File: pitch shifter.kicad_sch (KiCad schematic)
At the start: 16 parts, among them J1 MOLEX_430450412, J2 MOLEX_436500315, U2 STM32G030K8T6, U3 PCM3060PWR, Y1 ASE24LRT

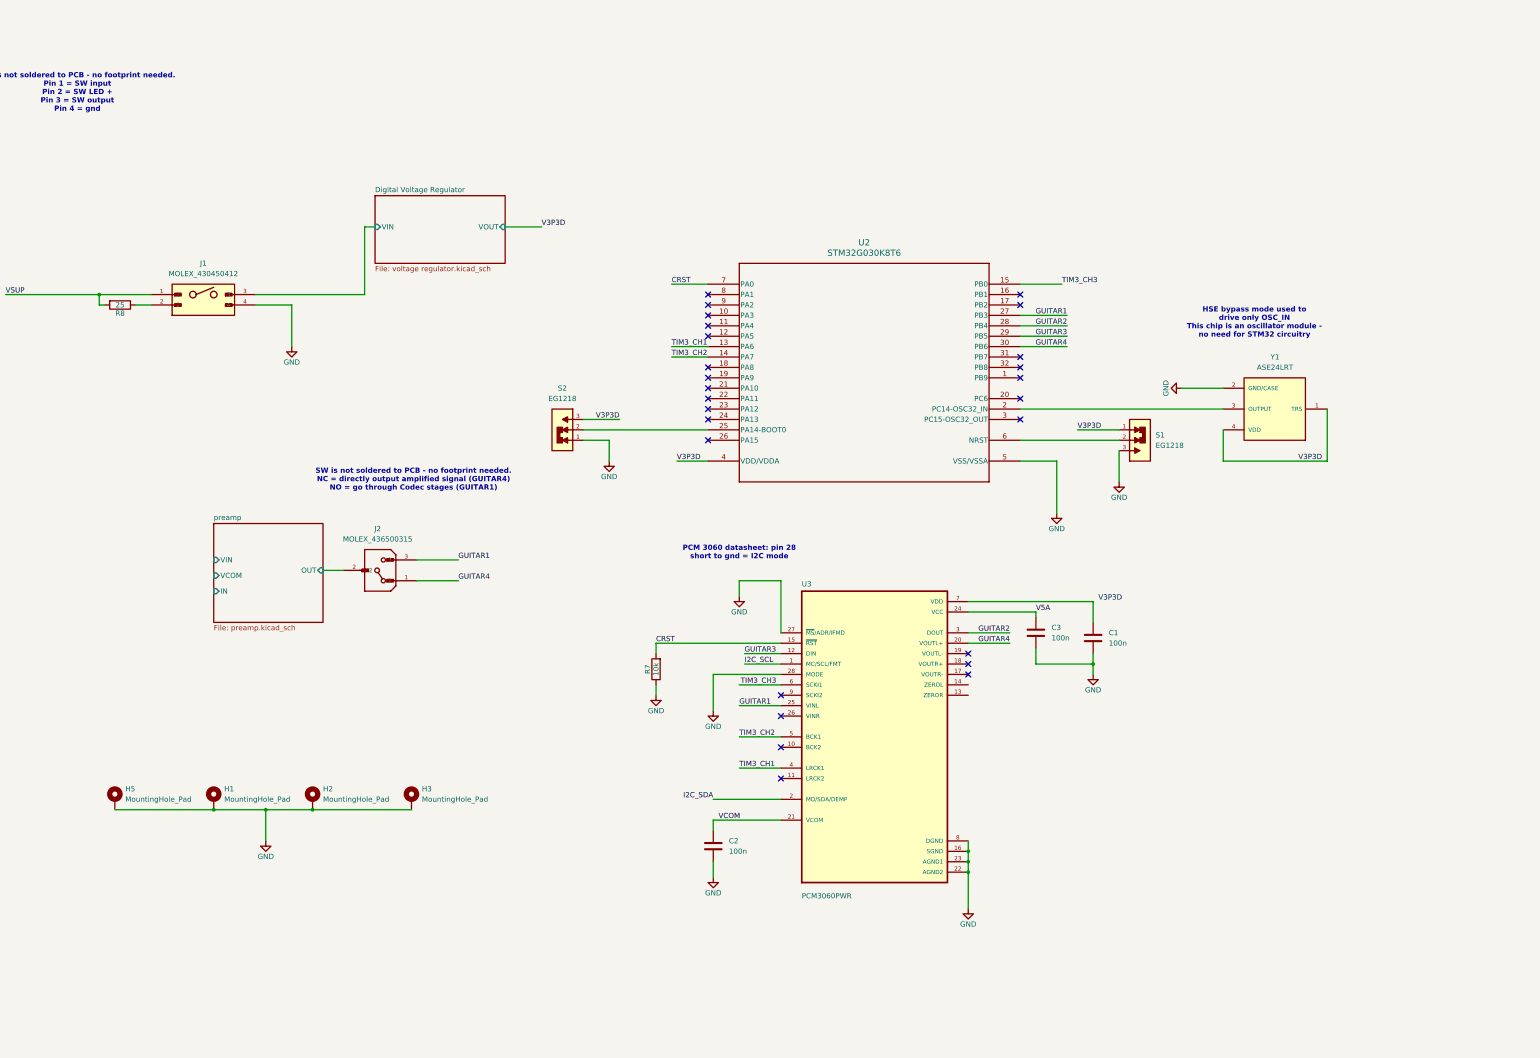
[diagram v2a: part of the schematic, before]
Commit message: Added analog supply, finished codec wiring, added audio jacks
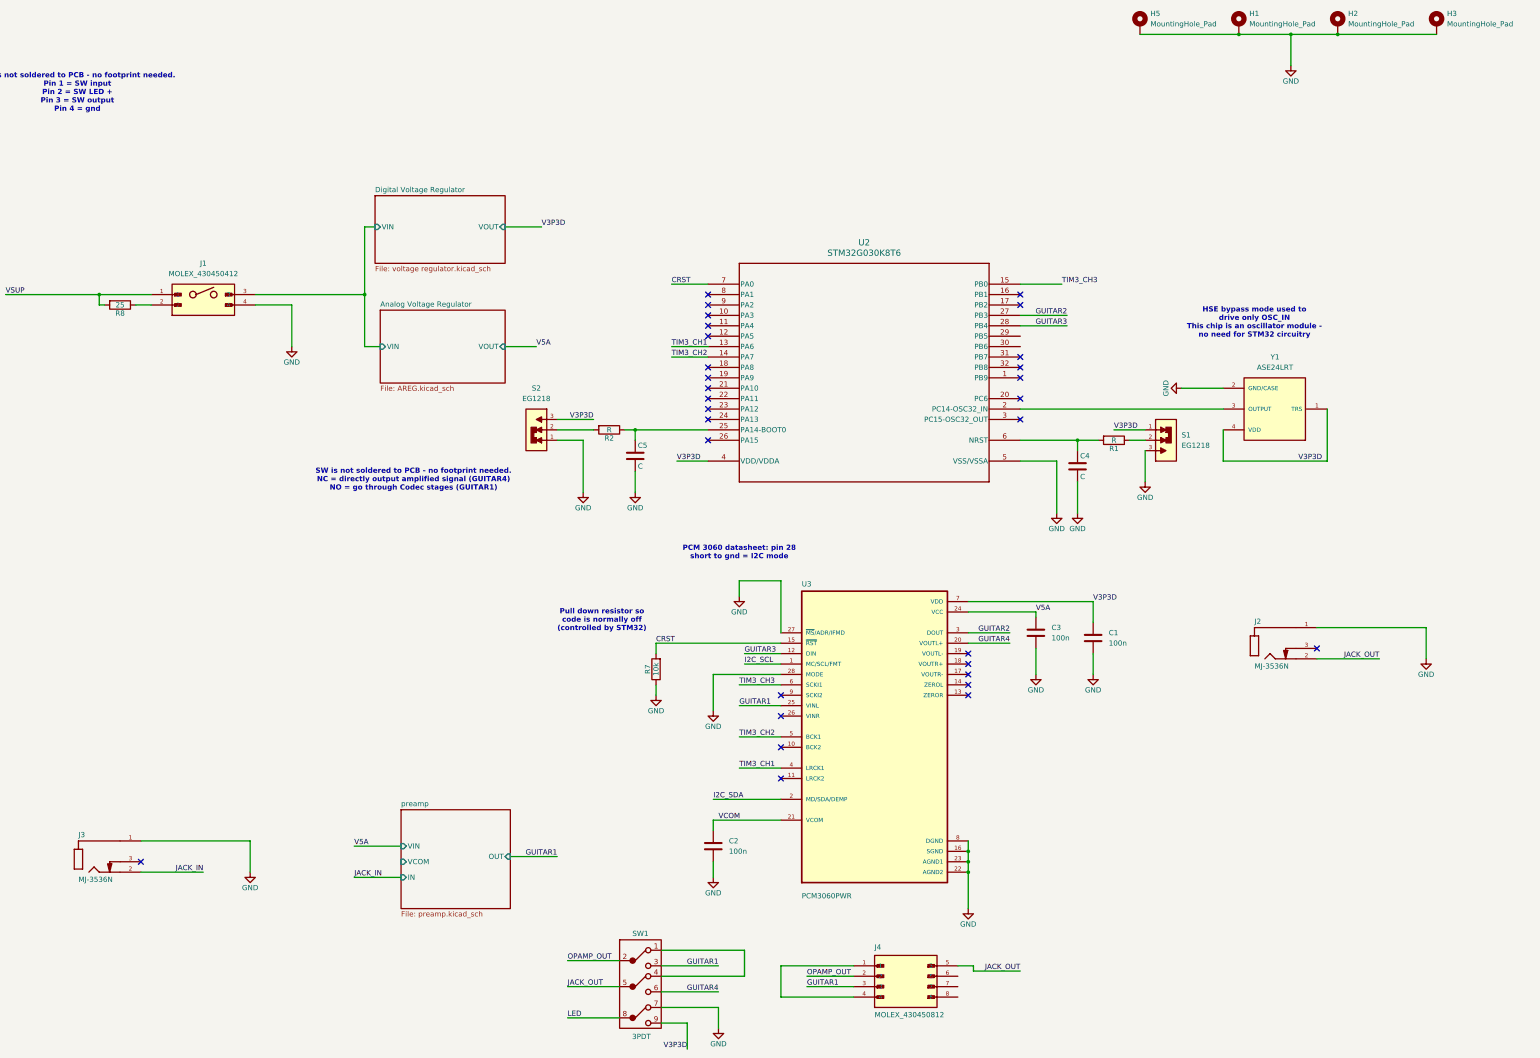
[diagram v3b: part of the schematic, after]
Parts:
- removed J2: MOLEX_436500315, Project_Components:MOLEX_436500315, symbol Project_Components:MOLEX_436500315
- added C4, C5: C, symbol Device:C
- added J2, J3: MJ-3536N, Project_Components:MJ-3536N, symbol Project_Components:MJ-3536N
- added J4: MOLEX_430450812, Project_Components:MOLEX_430450812, symbol Project_Components:MOLEX_430450812
- added R1, R2: R, symbol Device:R
- added SW1: 3PDT, symbol Project_Components:3PDT
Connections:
- net GND: now also C4.2, C5.2, J2.1, J3.1, SW1.7
- net GUITAR1: now also J4.3, SW1.3; no longer U2.27 (PB3)
- net GUITAR2: now also U2.27 (PB3); no longer U2.28 (PB4)
- net GUITAR3: now also U2.28 (PB4); no longer U2.29 (PB5)
- net GUITAR4: now also SW1.6; no longer U2.30 (PB6)
- net V3P3D: now also C1.1, U3.7 (VDD), SW1.9
- net at U2.25 (PA14-BOOT0): now also C5.1, R2.1; no longer S2.2
- net at S1.2: now also R1.1; no longer U2.6 (NRST)
- net Digital Voltage Regulator/VIN renamed Analog Voltage Regulator/VIN
- new net: C4.1, R1.2, U2.6 (NRST)
- new net: R2.2, S2.2
- new net: J4.1, J4.4
- new net: SW1.1, SW1.4
- new net JACK_IN: J3.2
- new net JACK_OUT: J2.2, J4.5, SW1.5
- new net LED: SW1.8
- new net OPAMP_OUT: J4.2, SW1.2
- no-connect marks 26 -> 30
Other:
- added sheet Analog Voltage Regulator (AREG.kicad_sch)
- note added: "Pull down resistor so code is normally off (controlled by STM32)"
- moved on the sheet: H1, H2, H3, H5, S1, S2

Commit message: swap stm32 with SAI compatible and add new molex connector
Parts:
- removed C5: C, symbol Device:C
- removed J4: MOLEX_430450812, Project_Components:MOLEX_430450812, symbol Project_Components:MOLEX_430450812
- removed R2: R, symbol Device:R
- removed S2: EG1218, Project_Components:EG1218, symbol Project_Components:EG1218
- removed U2: STM32G030K8T6, Project_Components:STM32G030K8T6, symbol Project_Components:STM32G030K8T6
- added C18: C, symbol Device:C
- added D3: D, symbol Device:D
- added J4: MOLEX_430450612, Project_Components:MOLEX_430450612, symbol Project_Components:MOLEX_430450612
- added R13, R14: R, symbol Device:R
- added S3: EG1218, Project_Components:EG1218, symbol Project_Components:EG1218
- added U6: STM32L432KCU6, Project_Components:STM32L432KCU6, symbol Project_Components:STM32L432KCU6
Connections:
- net GND: now also C18.2, D3.1 (K), S3.1, U6.16 (VSS), U6.32 (VSS__1); no longer SW1.7
- net GUITAR1: now also J4.2
- net GUITAR4: now also J4.4
- net JACK_OUT: now also J4.3
- net OPAMP_OUT: now also J4.1
- net V3P3D: now also J4.6, S3.3
- net at C4.1, R1.2: now also U6.4 (NRST)
- net at Y1.3 (OUTPUT): now also U6.2 (PC14-OSC32_1N)
- new net: C18.1, R14.2, U6.31 (PH3/BOOT0)
- new net: D3.2 (A), R13.1
- new net: J4.5, R13.2
- new net: R14.1, S3.2
- no-connect marks 30 -> 13
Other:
- note added: "This 3PDT switch is panel mounted (not on board) so it is merely a representation of the connections"
- moved on the sheet: C4, R1, S1, SW1, Y1

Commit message: Complete pre-amp and pre-amp sim
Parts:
- removed J1: MOLEX_430450412, Project_Components:MOLEX_430450412, symbol Project_Components:MOLEX_430450412
- removed J2, J3: MJ-3536N, Project_Components:MJ-3536N, symbol Project_Components:MJ-3536N
- removed R1: R, symbol Device:R
- removed S1, S3: EG1218, Project_Components:EG1218, symbol Project_Components:EG1218
- added C19: 1u, Capacitor_SMD:C_0201_0603Metric_Pad0.64x0.40mm_HandSolder, symbol Device:C
- added C20, C5: 10n, Capacitor_SMD:C_0201_0603Metric_Pad0.64x0.40mm_HandSolder, symbol Device:C
- added C21: 4.7u, Capacitor_SMD:C_0201_0603Metric_Pad0.64x0.40mm_HandSolder, symbol Device:C
- added C22: 100n, Capacitor_SMD:C_0201_0603Metric_Pad0.64x0.40mm_HandSolder, symbol Device:C
- added J5: SBH11-PBPC-D05-ST-BK, Project_Components:SBH11-PBPC-D05-ST-BK, symbol Project_Components:SBH11-PBPC-D05-ST-BK
- added R15, R2: 4.7k, symbol Device:R
- added SW2: PTS636, Project_Components:PTS636, symbol Project_Components:PTS636
- added SW3: EG1218, Project_Components:EG1218, symbol Project_Components:EG1218
- added SW5: SW_DPST, symbol Switch:SW_DPST
- C18, C4: value C -> 100n
- D3: footprint (none) -> Diode_SMD:D_0603_1608Metric_Pad1.05x0.95mm_HandSolder
- R13: value R -> 47
- R14: value R -> 10k
- R8: value 25 -> 47
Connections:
- net I2C_SCL is gone; now on net I2C_SCLK: U3.1 (MC/SCL/FMT)
- net TIM3_CH1 is gone; now on net WSCLK: U3.4 (LRCK1)
- net TIM3_CH2 is gone; now on net BLCK: U3.5 (BCK1)
- net TIM3_CH3 is gone; now on net SYSCLK: U3.6 (SCKI1)
- net Analog Voltage Regulator/VIN: now also SW5.4
- net CRST: now also U6.19 (PA9)
- net GND: now also U6.33 (EXP), C19.2, C20.2, C21.2, C22.2, C5.2, J5.5 (GND), J5.6 (GND), SW2.1 (A), SW3.1, SW5.2
- net GUITAR2: now also U6.20 (PA10)
- net GUITAR3: now also U6.28 (PB5)
- net I2C_SDA: now also U6.30 (PB7), R15.2
- net V3P3D: now also U6.1 (VDD), U6.17 (VDD__1), C20.1, C21.1, C22.1, J5.7 (3.3V), J5.8 (3.3V), R15.1, R2.1, SW3.3
- net V5A: now also U6.5 (VDDA/VREF+), C19.1, C5.1
- net VSUP: now also SW5.3
- net STRST: now reaches C4.1, U6.4 (NRST)
- net STRST: now also J5.1 (RST), SW2.2 (B)
- net SWDIO: now reaches U6.23 (PA13/JTMS-SWDIO)
- net SWDIO: now also J5.4 (SWDIO)
- net SWCLK: now reaches U6.24 (PA14/JTCK-SWCLK)
- net SWCLK: now also J5.2 (SWCLK)
- net I2C_SCLK: now reaches U6.29 (PB6)
- net I2C_SCLK: now also R2.2
- net WSCLK: now reaches U6.6 (PA0/CK_IN)
- net BLCK: now reaches U6.7 (PA1)
- net SYSCLK: now reaches U6.8 (PA2)
- net at R14.1: now also SW3.2
- net at R8.1: now also SW5.1
- no-connect marks 13 -> 27
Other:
- sheet preamp ports: added none; removed VCOM
- note added: "1 100n for each VDD pin"
- note added: "I2C pull up resistors"
- note added: "Pull down resistor so codec is normally off (controlled by STM32)"
- note removed: "Pull down resistor so code is normally off (controlled by STM32)"
- moved on the sheet: C18, C4, D3, R13, R14, R8, U6, Y1

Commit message: Began board layout
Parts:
- removed D3: D, Diode_SMD:D_0603_1608Metric_Pad1.05x0.95mm_HandSolder, symbol Device:D
- removed J4: MOLEX_430450612, Project_Components:MOLEX_430450612, symbol Project_Components:MOLEX_430450612
- removed R13: 47, symbol Device:R
- added D1: D, Diode_SMD:D_0603_1608Metric_Pad1.05x0.95mm_HandSolder, symbol Device:D
- added J1: TBL002A-4, Project_Components:TBL002A-4, symbol Project_Components:TBL002A-4
- added J2: USB4125-GF-A, Project_Components:USB-C (power only), symbol Project_Components:USB-C (power only)
- added J3: TBL002A-10, Project_Components:TBL002A-10, symbol Project_Components:TBL002A-10
- added R1, R5: 47, Resistor_SMD:R_0603_1608Metric_Pad0.98x0.95mm_HandSolder, symbol Device:R
- added R3, R4: 5.1k, Resistor_SMD:R_0603_1608Metric_Pad0.98x0.95mm_HandSolder, symbol Device:R
- added TP1, TP10, TP11, TP12, TP13, TP14, TP15, TP16, TP17, TP18, TP19, TP2, TP20, TP21, TP22, TP23, TP24, TP25, TP26, TP27, TP28, TP29, TP3, TP30, TP4, TP5, TP6, TP7, TP8, TP9: Test Point, TestPoint:TestPoint_THTPad_D1.0mm_Drill0.5mm, symbol Project_Components:Inline Test Point
- C1: renamed from C2; footprint Capacitor_SMD:C_0201_0603Metric_Pad0.64x0.40mm_HandSolder -> Capacitor_SMD:C_0603_1608Metric_Pad1.08x0.95mm_HandSolder
- C10: renamed from C21; footprint Capacitor_SMD:C_0201_0603Metric_Pad0.64x0.40mm_HandSolder -> Capacitor_SMD:C_0603_1608Metric_Pad1.08x0.95mm_HandSolder
- C2: renamed from C4; footprint (none) -> Capacitor_SMD:C_0603_1608Metric_Pad1.08x0.95mm_HandSolder
- C3: footprint Capacitor_SMD:C_0201_0603Metric_Pad0.64x0.40mm_HandSolder -> Capacitor_SMD:C_0603_1608Metric_Pad1.08x0.95mm_HandSolder
- C4: renamed from C1; footprint Capacitor_SMD:C_0201_0603Metric_Pad0.64x0.40mm_HandSolder -> Capacitor_SMD:C_0603_1608Metric_Pad1.08x0.95mm_HandSolder
- C5: renamed from C18; footprint (none) -> Capacitor_SMD:C_0603_1608Metric_Pad1.08x0.95mm_HandSolder
- C6: renamed from C22; footprint Capacitor_SMD:C_0201_0603Metric_Pad0.64x0.40mm_HandSolder -> Capacitor_SMD:C_0603_1608Metric_Pad1.08x0.95mm_HandSolder
- C7: renamed from C5; footprint Capacitor_SMD:C_0201_0603Metric_Pad0.64x0.40mm_HandSolder -> Capacitor_SMD:C_0603_1608Metric_Pad1.08x0.95mm_HandSolder
- C8: renamed from C20; value 10n -> 100n; footprint Capacitor_SMD:C_0201_0603Metric_Pad0.64x0.40mm_HandSolder -> Capacitor_SMD:C_0603_1608Metric_Pad1.08x0.95mm_HandSolder
- C9: renamed from C19; footprint Capacitor_SMD:C_0201_0603Metric_Pad0.64x0.40mm_HandSolder -> Capacitor_SMD:C_0603_1608Metric_Pad1.08x0.95mm_HandSolder
- R7: renamed from R2; footprint (none) -> Resistor_SMD:R_0603_1608Metric_Pad0.98x0.95mm_HandSolder
- R8: renamed from R14; footprint (none) -> Resistor_SMD:R_0603_1608Metric_Pad0.98x0.95mm_HandSolder
- R9: renamed from R15; footprint (none) -> Resistor_SMD:R_0603_1608Metric_Pad0.98x0.95mm_HandSolder
- renumbered H5 to H1, H1 to H2, H2 to H3, H3 to H4, J5 to J4, R8 to R2, R7 to R6, SW5 to SW1, SW1 to SW2, SW2 to SW3, SW3 to SW4, U6 to U1, U3 to U2
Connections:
- net BLCK: now also TP20.1
- net CRST: now also TP17.1
- net GND: now also D1.1 (K), J1.4, J2.A12 (GND), J2.B12 (GND__1), J2.S1 (SHIELD), J2.S2 (SHIELD__1), J2.S3 (SHIELD__2), J2.S4 (SHIELD__3), J3.2, J3.9, R3.2, R4.1
- net GUITAR1: now also J3.4, TP19.1
- net GUITAR2: now also U1.28 (PB5), TP26.1; no longer U1.20 (PA10)
- net GUITAR3: now also U1.20 (PA10), TP18.1; no longer U1.28 (PB5)
- net GUITAR4: now also J3.6, TP27.1
- net I2C_SCLK: now also TP29.1
- net I2C_SDA: now also TP22.1, TP30.1
- net JACK_IN: now also J3.1, TP6.1
- net JACK_OUT: now also J3.10, J3.5, TP5.1
- net LED: now also J3.7, R5.2, TP7.1
- net OPAMP_OUT: now also J3.3, TP14.1
- net STRST: now also TP10.1, TP25.1
- net SWCLK: now also TP15.1
- net SWDIO: now also TP13.1
- net SYSCLK: now also U1.6 (PA0/CK_IN), TP24.1; no longer U1.8 (PA2)
- net V3P3D: now also J3.8, TP11.1
- net V5A: now also TP12.1
- net VCOM: now also TP23.1
- net VSUP: now also J1.1, J2.A9 (VBUS), J2.B9 (VBUS__1), R1.1, TP1.1
- net WSCLK: now also U1.8 (PA2), TP21.1; no longer U1.6 (PA0/CK_IN)
- net at U1.2 (PC14-OSC32_1N), Y1.3 (OUTPUT): now also TP16.1
- net at C5.1, R8.2, U1.31 (PH3/BOOT0): now also TP28.1
- net at R2.1, SW1.1: now also TP4.1
- net Analog Voltage Regulator/VIN renamed VIN
- net VIN: now also J1.2, TP9.1
- new net: D1.2 (A), R5.1, TP8.1
- new net: J2.A5 (CC1), R4.2, TP3.1
- new net: J2.B5 (CC2), R3.1, TP2.1
- new net: J1.3, R1.2
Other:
- note added: "Pins 1-2, 9-10 belong to audio jack. Pins 3-8 belong to foot switch"
- moved on the sheet: C3, C4, H1, H2, H3, H4, SW2
